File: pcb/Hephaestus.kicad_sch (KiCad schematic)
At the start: 67 parts, among them J1 Fottpedal, J2 BT_ACTION, J3 USB_C_Receptacle_USB2.0, J4 PROG_CONN, J5 DBG_UART, J6 LED_CONN, Q1 AON7414, SW1 OLED_<, SW2 OLED_#, SW3 OLED_>, SW4 BT_RESET, U1 74HC14, U2 USBLC6-2SC6, U3 NCV8165ML330, U4 STM32L432KCUx, U5 M24C32, U6 OLED-128x32, U7 KTD2026BEWE

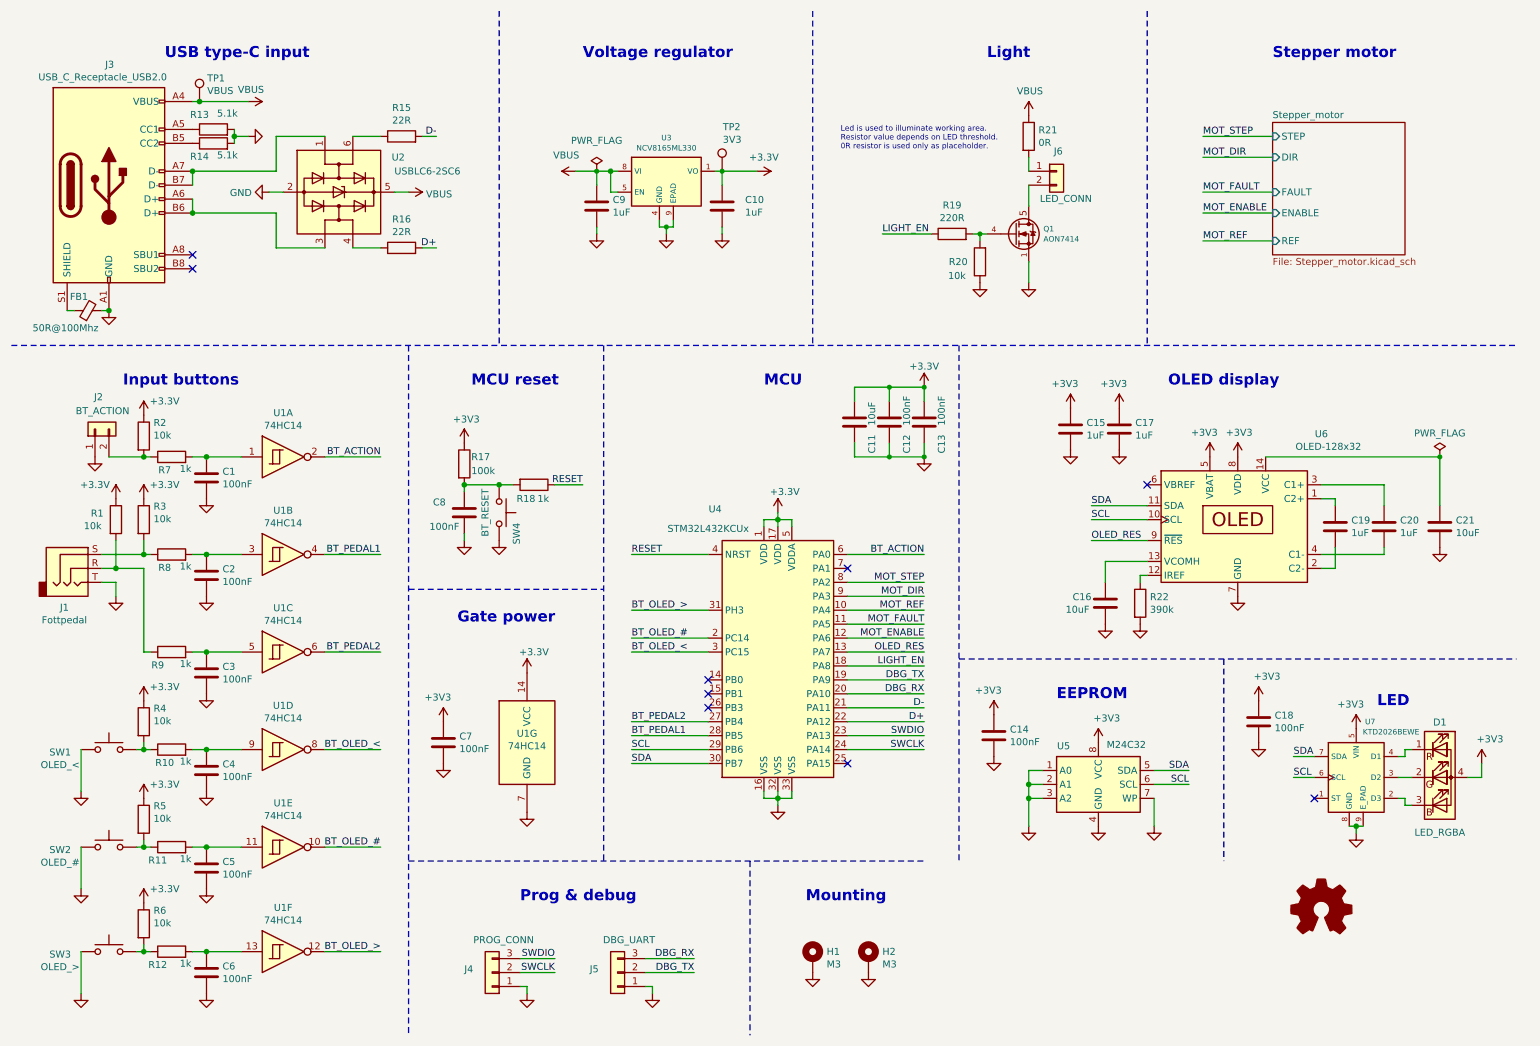
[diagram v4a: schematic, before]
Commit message: PCB: Basic routing done
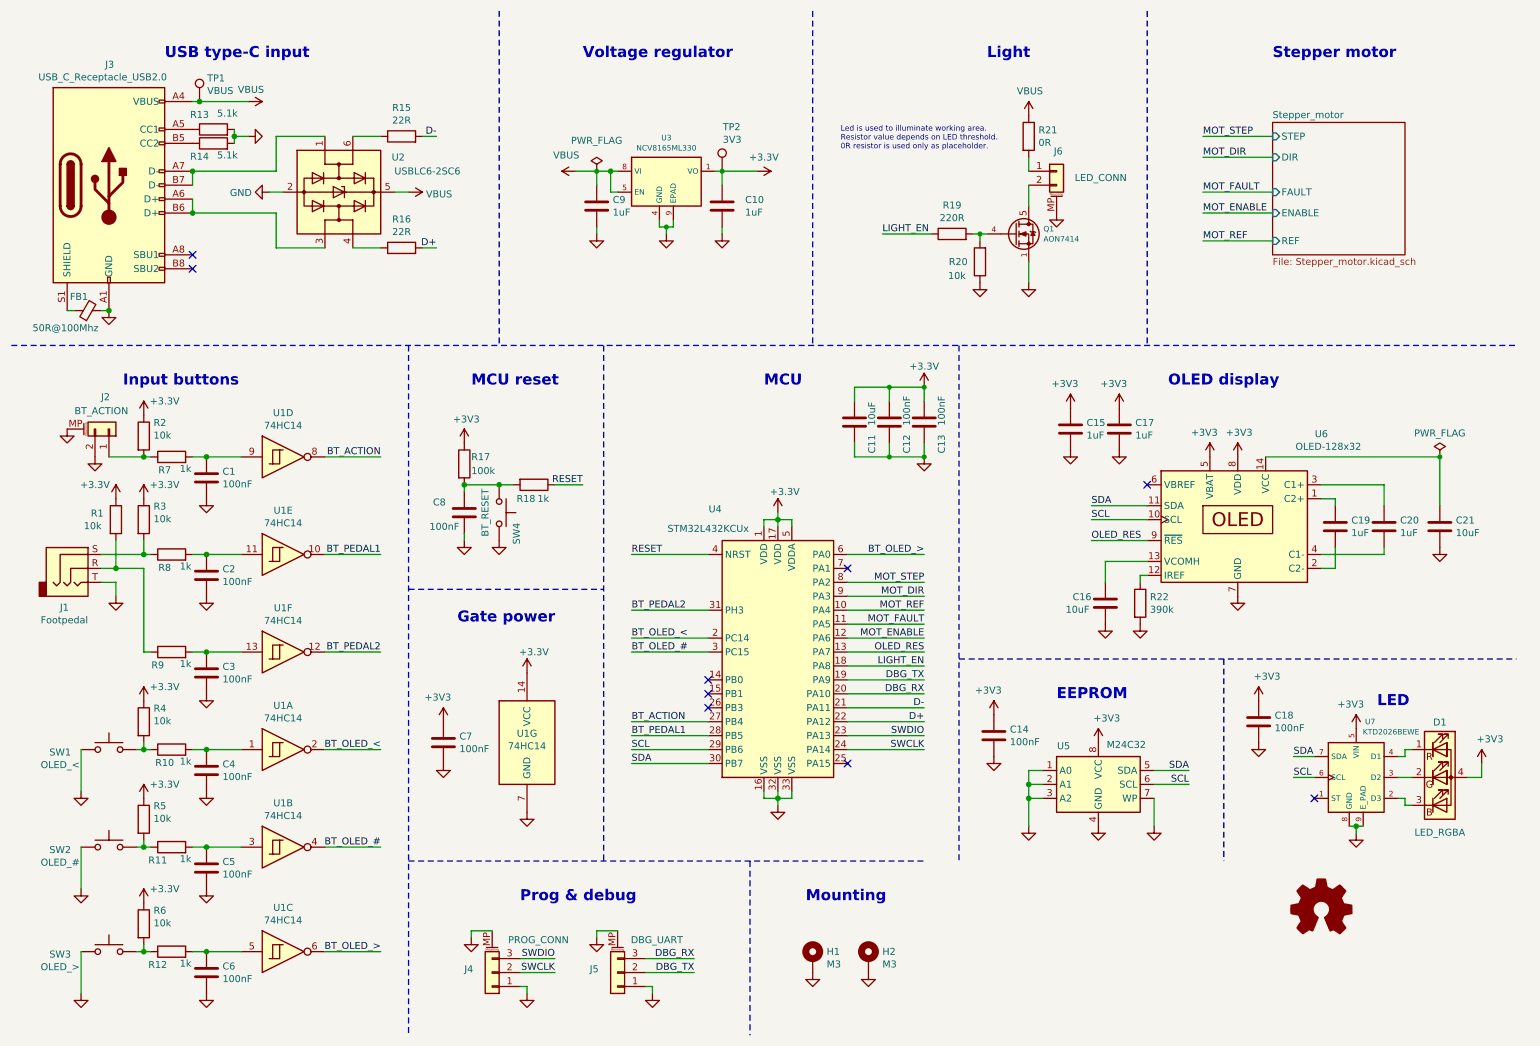
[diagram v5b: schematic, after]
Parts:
- C1, C2, C3, C4, C5, C6: footprint TCY_passives:C_0603_1608Metric -> Capacitor_SMD:C_0603_1608Metric
- J1: value Fottpedal -> Footpedal
- J2, J6: symbol Connector_Generic:Conn_01x02 -> Connector_Generic_MountingPin:Conn_01x02_MountingPin
- J4, J5: symbol Connector_Generic:Conn_01x03 -> Connector_Generic_MountingPin:Conn_01x03_MountingPin
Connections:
- net BT_ACTION: now also U1.8, U4.27 (PB4); no longer U1.2, U4.6 (PA0)
- net BT_OLED_#: now also U1.4, U4.3 (PC15); no longer U1.10, U4.2 (PC14)
- net BT_OLED_<: now also U1.2, U4.2 (PC14); no longer U1.8, U4.3 (PC15)
- net BT_OLED_>: now also U1.6, U4.6 (PA0); no longer U1.12, U4.31 (PH3)
- net BT_PEDAL1: now also U1.10; no longer U1.4
- net BT_PEDAL2: now also U1.12, U4.31 (PH3); no longer U1.6, U4.27 (PB4)
- net GND: now also J2.2 (Pin_2), J2.MP (MountPin), J4.MP (MountPin), J5.MP (MountPin), J6.MP (MountPin); no longer J2.1 (Pin_1)
- net at C4.1, R10.2: now also U1.1; no longer U1.9
- net at C5.1, R11.2: now also U1.3; no longer U1.11
- net at C3.1, R9.2: now also U1.13; no longer U1.5
- net at R2.2, R7.1: now also J2.1 (Pin_1); no longer J2.2 (Pin_2)
- net at C1.1, R7.2: now also U1.9; no longer U1.1
- net at C6.1, R12.2: now also U1.5; no longer U1.13
- net at C2.1, R8.2: now also U1.11; no longer U1.3
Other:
- moved on the sheet: U1A, U1B, U1C, U1D, U1E, U1F
